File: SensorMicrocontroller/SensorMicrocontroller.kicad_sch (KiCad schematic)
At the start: 2 parts, among them J1 JST B6B-PH-SM4-TB, U1 SC0915

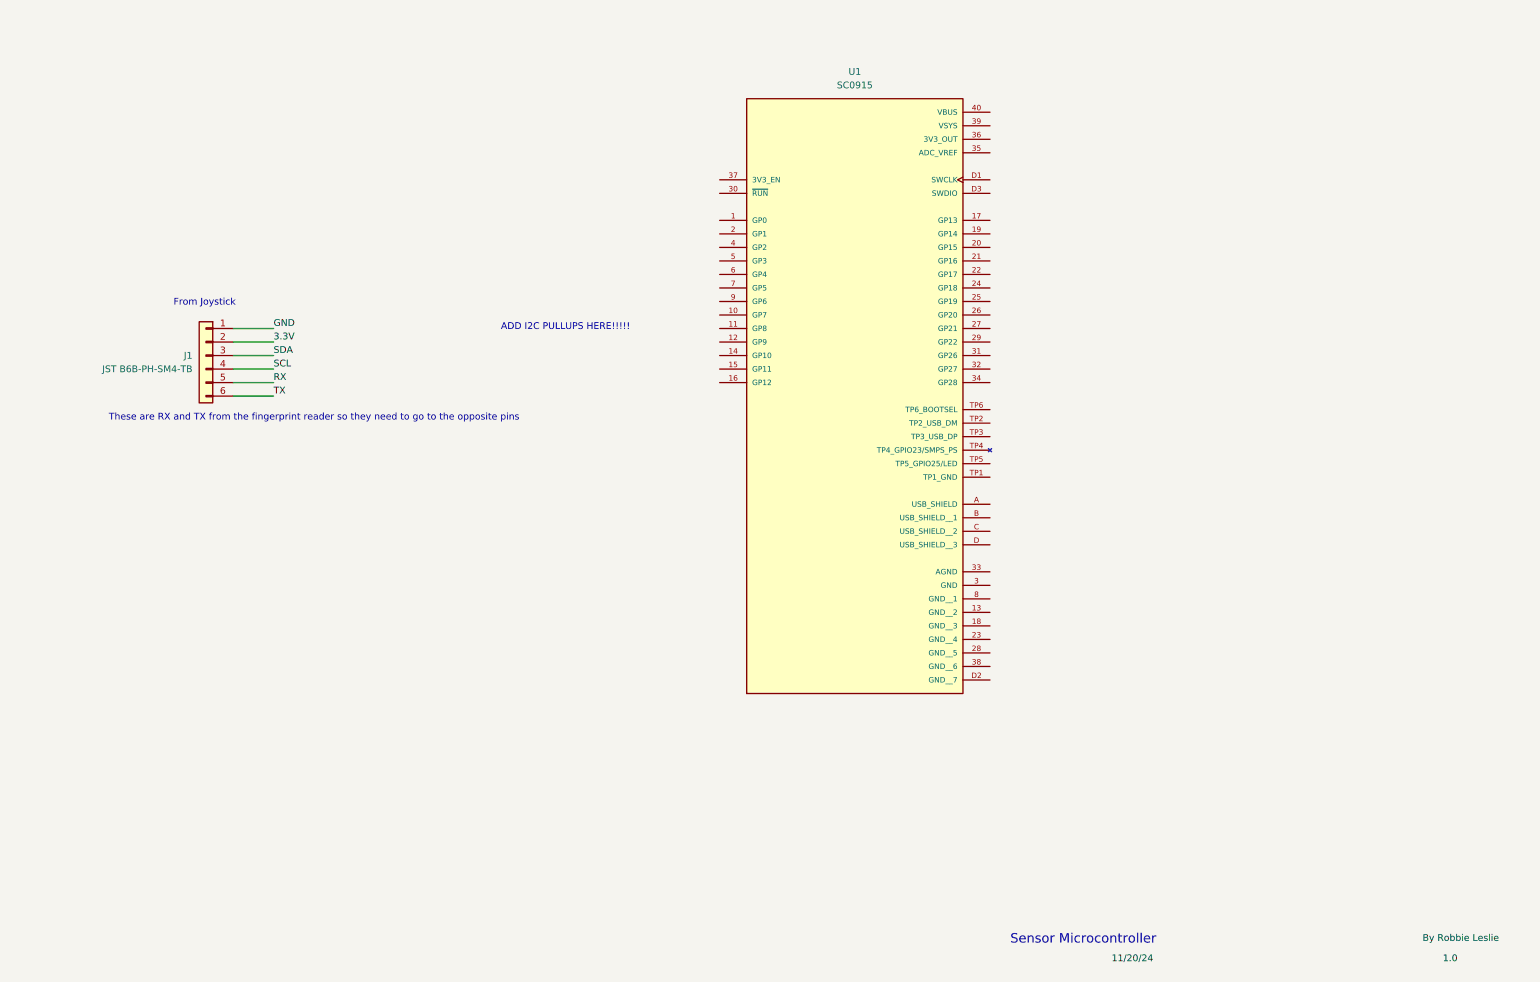
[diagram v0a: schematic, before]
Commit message: Started work on ultrasonic ADC
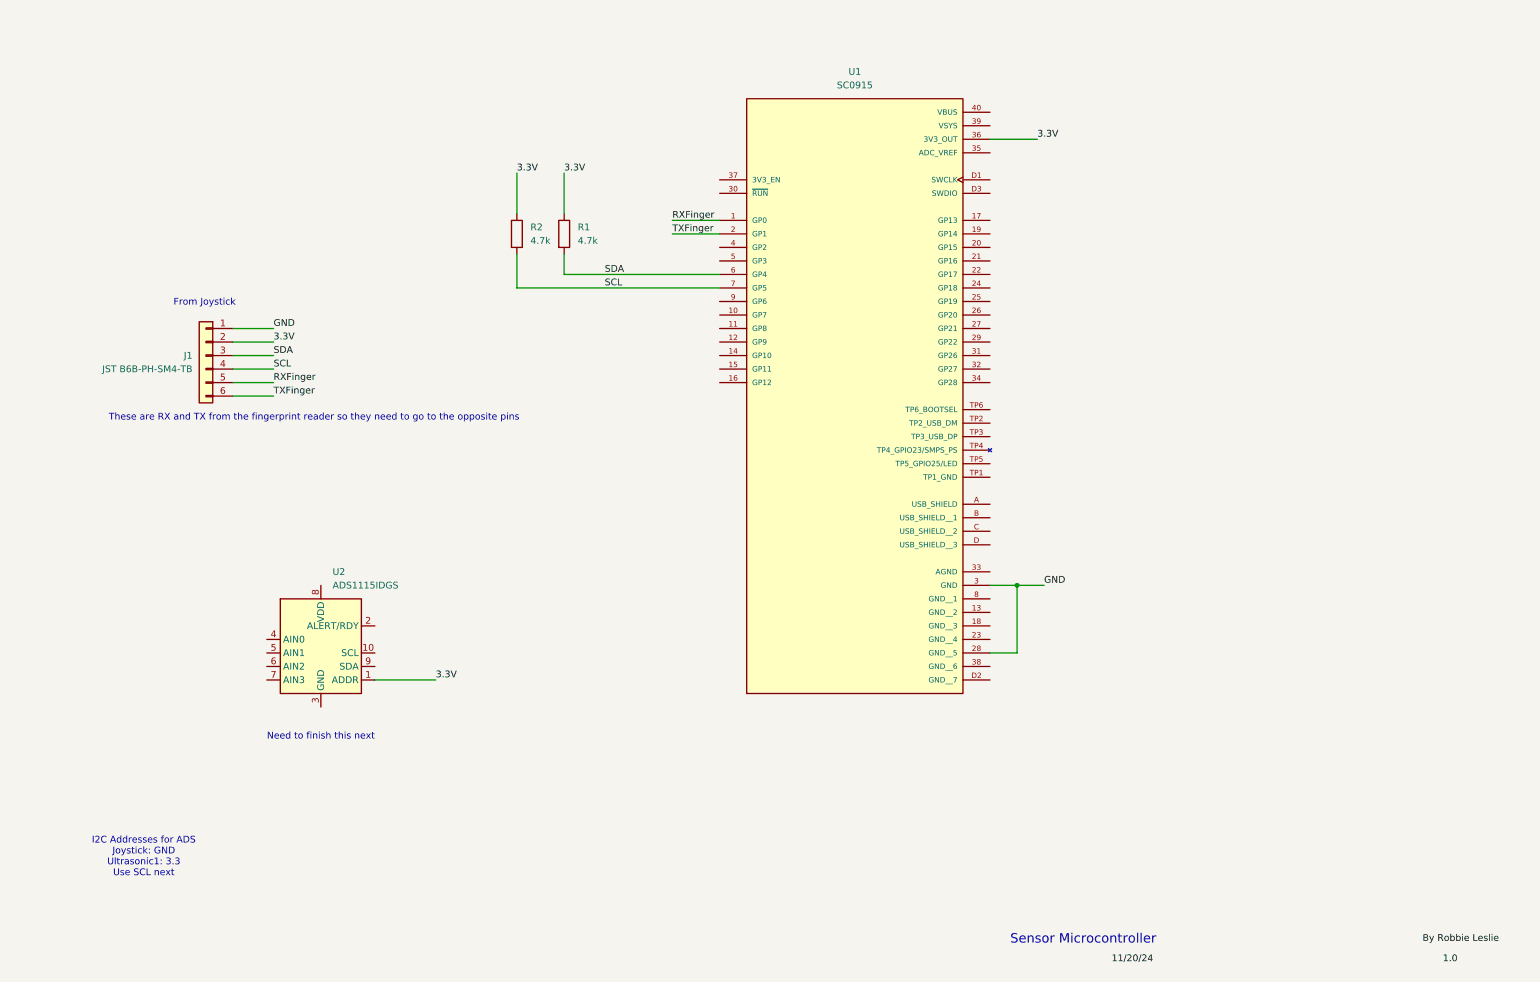
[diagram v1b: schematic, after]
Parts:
- added R1, R2: 4.7k, Resistor_SMD:R_0805_2012Metric, symbol Device:R
- added U2: ADS1115IDGS, Package_SO:TSSOP-10_3x3mm_P0.5mm, symbol Analog_ADC:ADS1115IDGS
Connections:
- net RX is gone; now on net RXFinger: J1.5 (Pin_5)
- net TX is gone; now on net TXFinger: J1.6 (Pin_6)
- net 3.3V: now also U1.36 (3V3_OUT), R1.1, R2.1, U2.1 (ADDR)
- net GND: now also U1.28 (GND__5), U1.3 (GND)
- net SCL: now also U1.7 (GP5), R2.2
- net SDA: now also U1.6 (GP4), R1.2
- net RXFinger: now reaches U1.1 (GP0)
- net TXFinger: now reaches U1.2 (GP1)
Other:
- note added: "I2C Addresses for ADS Joystick: GND Ultrasonic1: 3.3 Use SCL next"
- note added: "Need to finish this next"
- note removed: "ADD I2C PULLUPS HERE!!!!!"

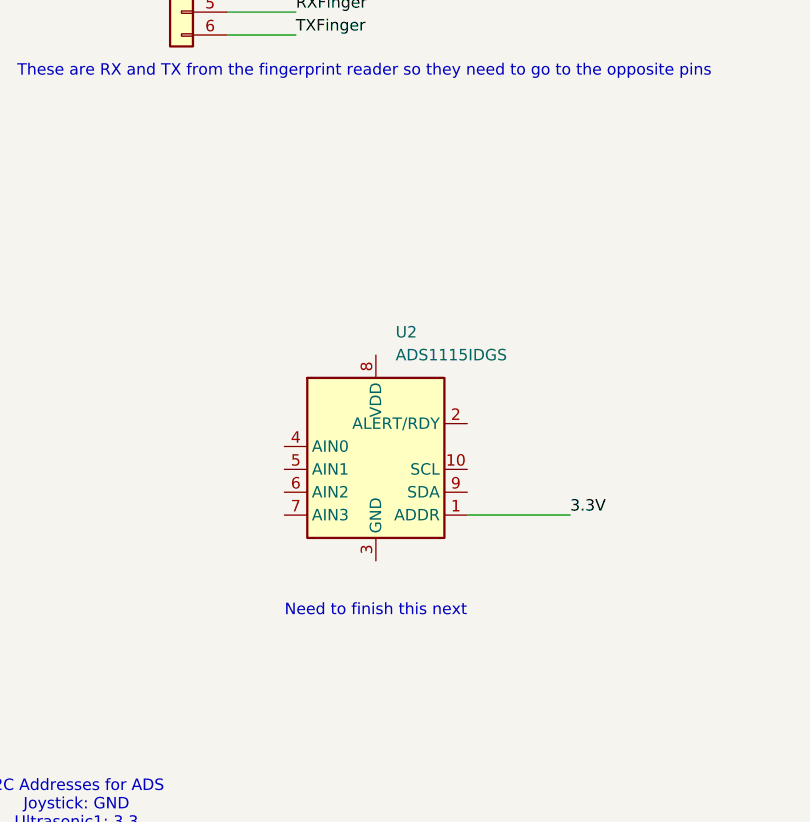
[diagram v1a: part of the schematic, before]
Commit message: Worked on power for ADS0
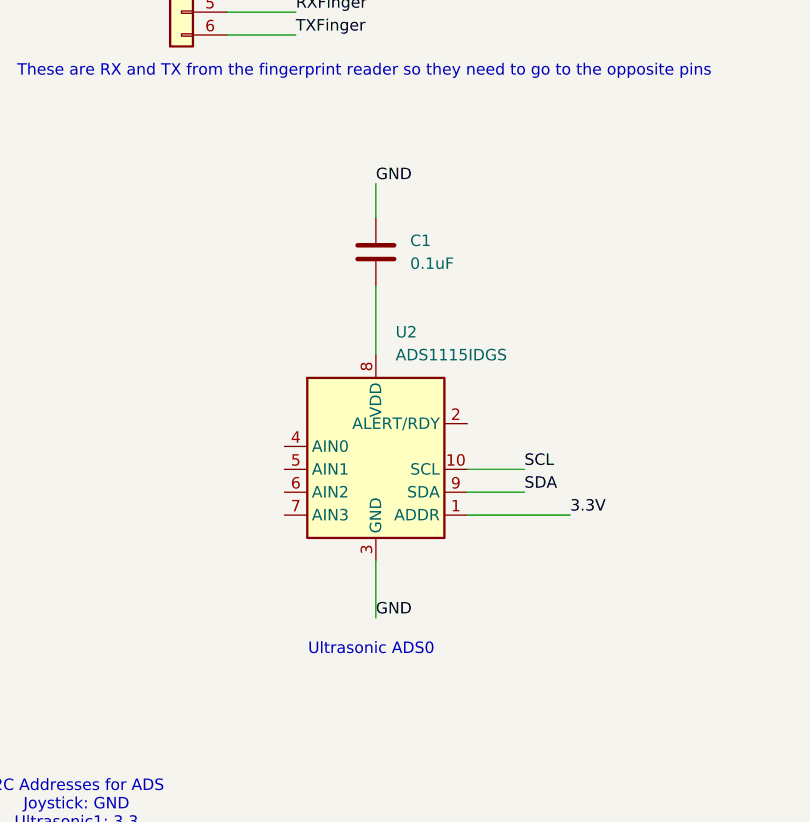
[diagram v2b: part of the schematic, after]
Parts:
- added C1: 0.1uF, Capacitor_SMD:C_0805_2012Metric, symbol Device:C
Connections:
- net GND: now also U2.3 (GND), C1.1
- net SCL: now also U2.10 (SCL)
- net SDA: now also U2.9 (SDA)
- net at U2.8 (VDD): now also C1.2
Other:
- note added: "Ultrasonic ADS0"
- note removed: "Need to finish this next"
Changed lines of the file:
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@@
+	(wire
+		(pts
+			(xy 58.42 115.57) (xy 58.42 123.19)
+		)
+		(stroke
+			(width 0)
+			(type default)
+		)
+	)
 	(wire
 		(pts
@@
 	(wire
 		(pts
+			(xy 58.42 146.05) (xy 58.42 152.4)
+		)
+		(stroke
+			(width 0)
+			(type default)
+		)
+	)
+	(wire
+		(pts
 			(xy 41.91 80.01) (xy 49.53 80.01)
 		)
@@
 		(pts
 			(xy 41.91 85.09) (xy 49.53 85.09)
+		)
+		(stroke
+			(width 0)
+			(type default)
+		)
+	)
+	(wire
+		(pts
+			(xy 68.58 135.89) (xy 74.93 135.89)
+		)
+		(stroke
+			(width 0)
+			(type default)
+		)
+	)
+	(wire
+		(pts
+			(xy 58.42 104.14) (xy 58.42 107.95)
+		)
+		(stroke
+			(width 0)
+			(type default)
+		)
+	)
+	(wire
+		(pts
+			(xy 68.58 138.43) (xy 74.93 138.43)
 		)
 		(stroke
@@
 		)
 	)
-	(text "Need to finish this next"
+	(text "Ultrasonic ADS0"
 		(exclude_from_sim no)
-		(at 58.42 151.638 0)
+		(at 57.912 155.956 0)
 		(effects
 			(font
@@
 		)
 	)
+	(label "GND"
+		(at 58.42 104.14 0)
+		(fields_autoplaced yes)
+		(effects
+			(font
+				(size 1.27 1.27)
+			)
+			(justify left bottom)
+		)
+	)
 	(label "SDA"
 		(at 111.76 64.77 0)
@@
 		)
 	)
+	(label "SDA"
+		(at 74.93 138.43 0)
+		(fields_autoplaced yes)
+		(effects
+			(font
+				(size 1.27 1.27)
+			)
+			(justify left bottom)
+		)
+	)
 	(label "1.0"
 		(at 269.24 194.31 0)
@@
 		)
 	)
+	(label "SCL"
+		(at 74.93 135.89 0)
+		(fields_autoplaced yes)
+		(effects
+			(font
+				(size 1.27 1.27)
+			)
+			(justify left bottom)
+		)
+	)
 	(label "3.3V"
 		(at 193.04 39.37 0)
@@
 	(label "GND"
 		(at 194.31 123.19 0)
+		(fields_autoplaced yes)
+		(effects
+			(font
+				(size 1.27 1.27)
+			)
+			(justify left bottom)
+		)
+	)
+	(label "GND"
+		(at 58.42 152.4 0)
 		(fields_autoplaced yes)
 		(effects
@@
 					(unit 1)
 				)
+			)
+		)
+	)
+	(symbol
+		(lib_id "Device:C")
+		(at 58.42 111.76 0)
+		(unit 1)
+		(exclude_from_sim no)
+		(in_bom yes)
+		(on_board yes)
+		(dnp no)
+		(fields_autoplaced yes)
+		(property "Reference" "C1"
+			(at 62.23 110.4899 0)
+			(effects
+				(font
+					(size 1.27 1.27)
+				)
+				(justify left)
+			)
+		)
+		(property "Value" "0.1uF"
+			(at 62.23 113.0299 0)
+			(effects
+				(font
+					(size 1.27 1.27)
+				)
+				(justify left)
+			)
+		)
+		(property "Footprint" "Capacitor_SMD:C_0805_2012Metric"
+			(at 59.3852 115.57 0)
+			(effects
+				(font
+					(size 1.27 1.27)
+				)
+				(hide yes)
+			)
+		)
+		(property "Datasheet" "~"
+			(at 58.42 111.76 0)
+			(effects
+				(font
+					(size 1.27 1.27)
+				)
+				(hide yes)
+			)
+		)
+		(property "Description" "Unpolarized capacitor"
+			(at 58.42 111.76 0)
+			(effects
+				(font
+					(size 1.27 1.27)
+				)
+				(hide yes)
+			)
+		)
+		(pin "2"
+		)
+		(pin "1"
+		)
+		(instances
+			(project ""
+				(path "/13d126c3-058e-4769-8500-e0ab3b4ccece"
+					(reference "C1")
+					(unit 1)
+				)

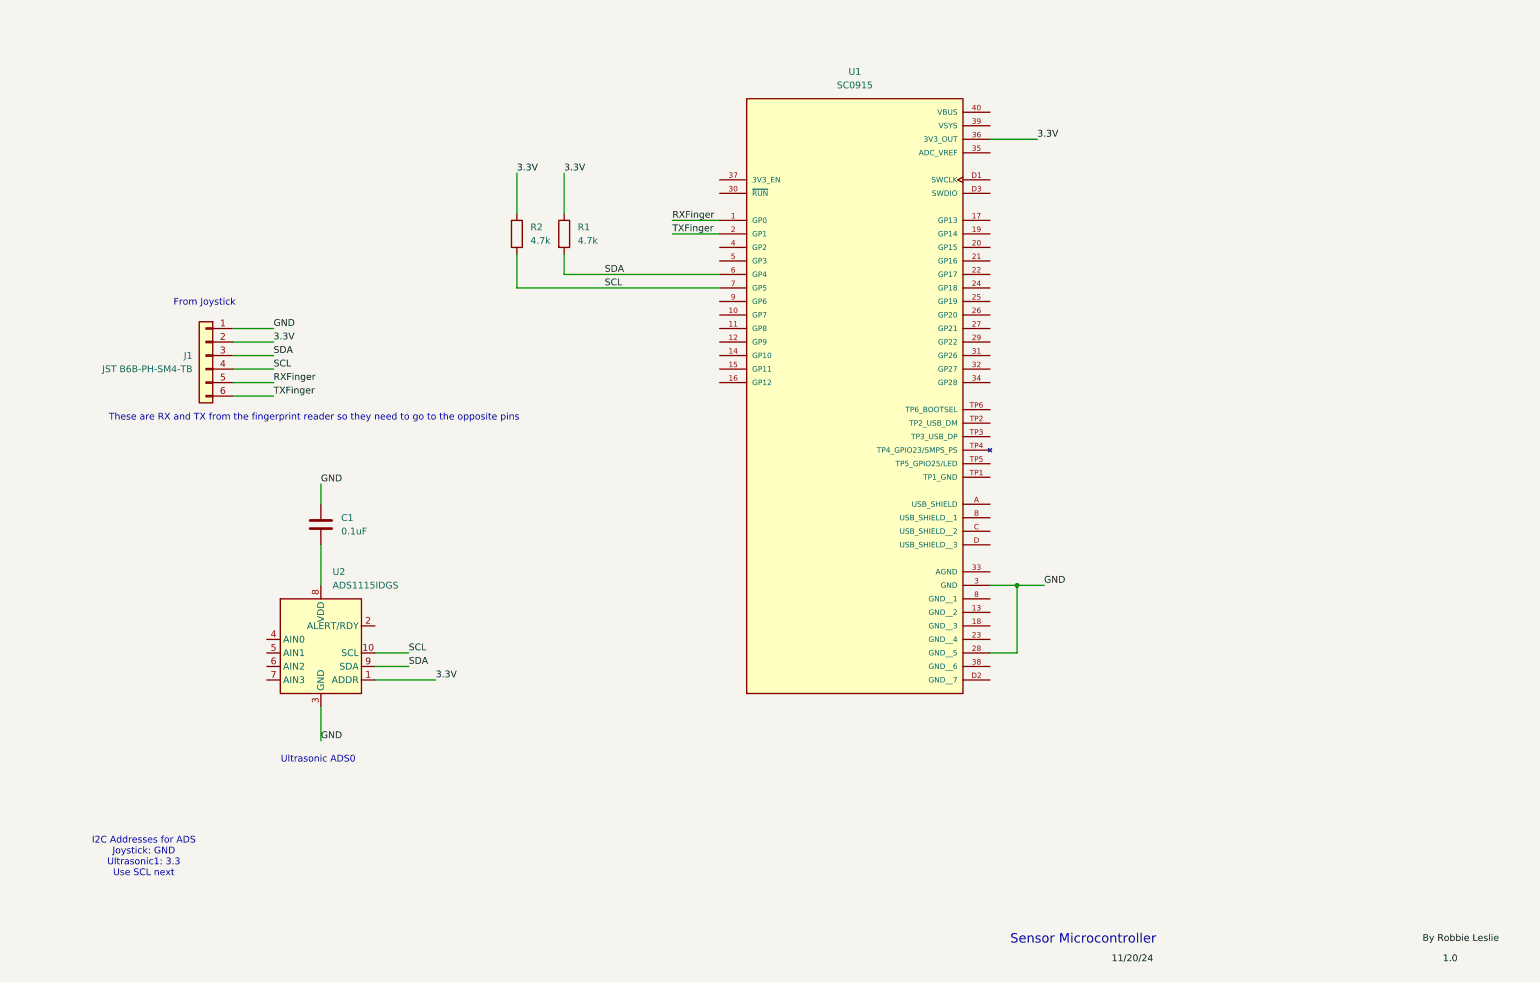
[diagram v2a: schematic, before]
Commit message: Added connectors for ultrasonic + PIR boards
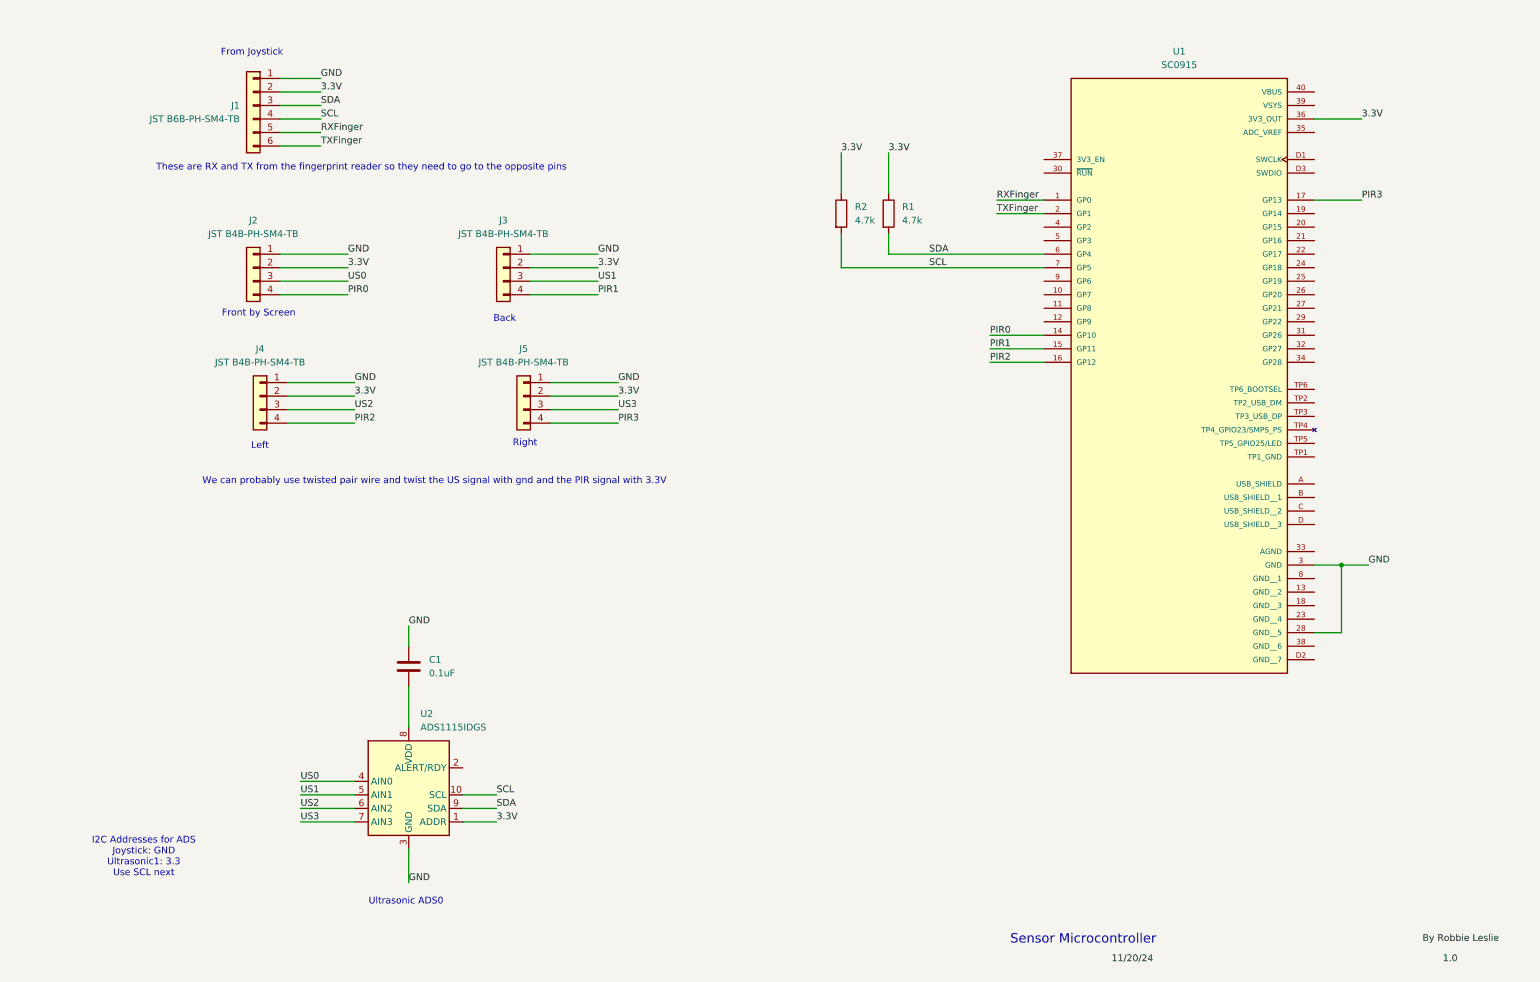
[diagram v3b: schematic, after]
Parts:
- added J2, J3, J4, J5: JST B4B-PH-SM4-TB, Connector_JST:JST_PH_B4B-PH-SM4-TB_1x04-1MP_P2.00mm_Vertical, symbol Connector_Generic:Conn_01x04
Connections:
- net 3.3V: now also J2.2 (Pin_2), J3.2 (Pin_2), J4.2 (Pin_2), J5.2 (Pin_2)
- net GND: now also J2.1 (Pin_1), J3.1 (Pin_1), J4.1 (Pin_1), J5.1 (Pin_1)
- net US0: now reaches U2.4 (AIN0)
- net US0: now also J2.3 (Pin_3)
- net US1: now reaches U2.5 (AIN1)
- net US1: now also J3.3 (Pin_3)
- net US2: now reaches U2.6 (AIN2)
- net US2: now also J4.3 (Pin_3)
- net US3: now reaches U2.7 (AIN3)
- net US3: now also J5.3 (Pin_3)
- net PIR0: now reaches U1.14 (GP10)
- net PIR0: now also J2.4 (Pin_4)
- net PIR1: now reaches U1.15 (GP11)
- net PIR1: now also J3.4 (Pin_4)
- net PIR2: now reaches U1.16 (GP12)
- net PIR2: now also J4.4 (Pin_4)
- net PIR3: now reaches U1.17 (GP13)
- net PIR3: now also J5.4 (Pin_4)
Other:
- note added: "Back"
- note added: "Front by Screen"
- note added: "Left"
- note added: "Right"
- note added: "We can probably use twisted pair wire and twist the US signal with gnd and the PIR signal with 3.3V"
- moved on the sheet: C1, J1, R1, R2, U1, U2
